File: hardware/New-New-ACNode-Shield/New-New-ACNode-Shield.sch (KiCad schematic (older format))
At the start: 6 parts, among them J1 8P8C_Shielded, J2 8P8C_Shielded, U1 ISL3176EIBZ, U2 EK-TM4C1294XL

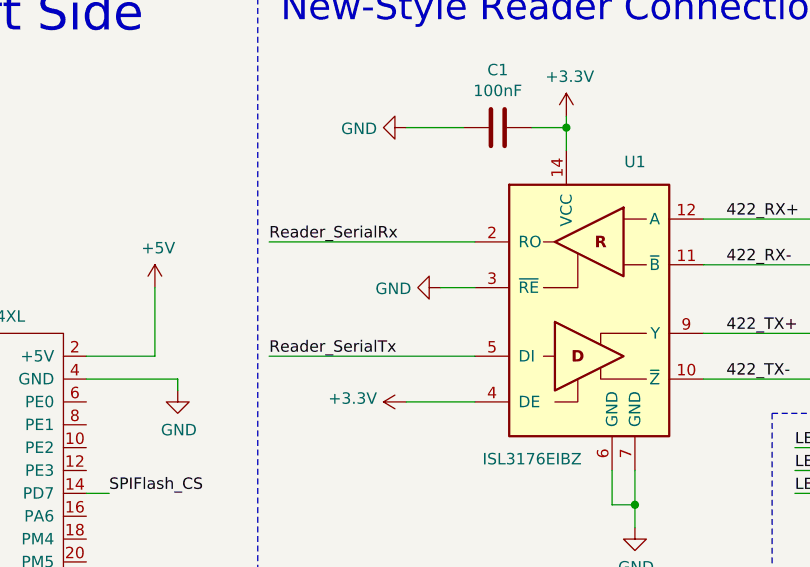
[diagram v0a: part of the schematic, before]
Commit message: Slightly reworked New-New-ACNode-Shield
The ethernet connector was fouling the PCB, so this
is an attempt to create a suitable cutout. It involves moving the tool running detection.
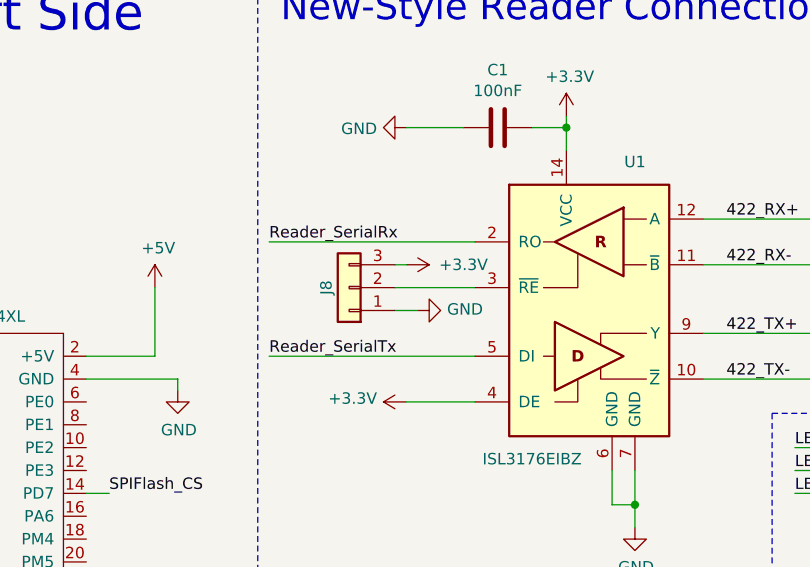
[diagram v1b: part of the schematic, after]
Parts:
- added J8: Conn_01x03, Connector_PinHeader_2.54mm:PinHeader_1x03_P2.54mm_Vertical, symbol Connector_Generic:Conn_01x03
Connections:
- wire segments 84 -> 86
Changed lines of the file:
@@
 L power:GND #PWR0112
 U 1 1 5FC29A42
-P 4050 1900
-F 0 "#PWR0112" H 4050 1650 50  0001 C CNN
-F 1 "GND" V 4055 1772 50  0000 R CNN
-F 2 "" H 4050 1900 50  0001 C CNN
-F 3 "" H 4050 1900 50  0001 C CNN
-	1    4050 1900
-	0    1    1    0
+P 3950 2000
+F 0 "#PWR0112" H 3950 1750 50  0001 C CNN
+F 1 "GND" V 3955 1872 50  0000 R CNN
+F 2 "" H 3950 2000 50  0001 C CNN
+F 3 "" H 3950 2000 50  0001 C CNN
+	1    3950 2000
+	0    -1   -1   0
 $EndComp
 $Comp
@@
 	0    -1   -1   0
 $EndComp
-Wire Wire Line
-	4200 1900 4050 1900
 Wire Wire Line
 	4200 2400 3900 2400
@@
 Wire Wire Line
 	10400 6050 10500 6050
+$Comp
+L Connector_Generic:Conn_01x03 J8
+U 1 1 6111755B
+P 3650 1900
+F 0 "J8" V 3750 1900 50  0000 C CNN
+F 1 "Conn_01x03" H 3600 2100 50  0001 C CNN
+F 2 "Connector_PinHeader_2.54mm:PinHeader_1x03_P2.54mm_Vertical" H 3650 1900 50  0001 C CNN
+F 3 "~" H 3650 1900 50  0001 C CNN
+	1    3650 1900
+	-1   0    0    1
+$EndComp
+$Comp
+L power:+3.3V #PWR0105
+U 1 1 6112247B
+P 3900 1800
+F 0 "#PWR0105" H 3900 1650 50  0001 C CNN
+F 1 "+3.3V" V 3900 2050 50  0000 C CNN
+F 2 "" H 3900 1800 50  0001 C CNN
+F 3 "" H 3900 1800 50  0001 C CNN
+	1    3900 1800
+	0    1    1    0
+$EndComp
+Wire Wire Line
+	4200 1900 3850 1900
+Wire Wire Line
+	3850 2000 3950 2000
+Wire Wire Line
+	3900 1800 3850 1800
 $EndSCHEMATC
